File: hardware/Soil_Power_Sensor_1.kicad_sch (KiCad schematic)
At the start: 24 parts, among them J1 Screw_Terminal_01x05, J4 Rsense, U1 THS4532, U2 MAX9944, U3 INA296A, U4 ADS1219

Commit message: Updated board layout
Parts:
- removed J4: Rsense, Connector_PinHeader_2.54mm:PinHeader_1x02_P2.54mm_Vertical, symbol Connector:Conn_01x02_Socket
- RSENSE1: value NC -> DNP
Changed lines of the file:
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@@
   (junction (at 121.92 113.03) (diameter 0) (color 0 0 0 0)
   )
-  (junction (at 35.56 142.24) (diameter 0) (color 0 0 0 0)
-  )
   (junction (at 185.42 99.06) (diameter 0) (color 0 0 0 0)
   )
@@
   (junction (at 87.63 22.86) (diameter 0) (color 0 0 0 0)
   )
-  (junction (at 35.56 132.08) (diameter 0) (color 0 0 0 0)
-  )
   (junction (at 185.42 91.44) (diameter 0) (color 0 0 0 0)
   )
@@
     (stroke (width 0.1524) (type solid))
   )
-  (wire (pts (xy 20.32 132.08) (xy 35.56 132.08))
-    (stroke (width 0) (type default))
-  )
   (wire (pts (xy 124.46 130.81) (xy 121.92 130.81))
     (stroke (width 0.1524) (type solid))
@@
     (stroke (width 0) (type default))
   )
-  (wire (pts (xy 35.56 132.08) (xy 35.56 133.35))
-    (stroke (width 0.1524) (type solid))
-  )
   (wire (pts (xy 254 71.12) (xy 254 73.66))
     (stroke (width 0.1524) (type solid))
@@
     (stroke (width 0.1524) (type solid))
   )
-  (wire (pts (xy 35.56 124.46) (xy 35.56 132.08))
+  (wire (pts (xy 35.56 124.46) (xy 35.56 133.35))
     (stroke (width 0.1524) (type solid))
   )
@@
     (stroke (width 0.1524) (type solid))
   )
-  (wire (pts (xy 20.32 135.89) (xy 20.32 132.08))
-    (stroke (width 0) (type default))
-  )
   (wire (pts (xy 92.71 116.84) (xy 92.71 119.38))
     (stroke (width 0) (type default))
@@
     (stroke (width 0.1524) (type solid))
   )
-  (wire (pts (xy 35.56 140.97) (xy 35.56 142.24))
-    (stroke (width 0.1524) (type solid))
-  )
   (wire (pts (xy 48.26 99.06) (xy 48.26 149.86))
     (stroke (width 0.1524) (type solid))
@@
     (stroke (width 0.1524) (type solid))
   )
-  (wire (pts (xy 20.32 142.24) (xy 35.56 142.24))
-    (stroke (width 0) (type default))
-  )
   (wire (pts (xy 144.78 52.07) (xy 162.56 52.07))
     (stroke (width 0.1524) (type solid))
   )
-  (wire (pts (xy 35.56 142.24) (xy 35.56 149.86))
+  (wire (pts (xy 35.56 140.97) (xy 35.56 149.86))
     (stroke (width 0.1524) (type solid))
   )
   (wire (pts (xy 231.14 71.12) (xy 236.22 71.12))
     (stroke (width 0.1524) (type solid))
-  )
-  (wire (pts (xy 20.32 138.43) (xy 20.32 142.24))
-    (stroke (width 0) (type default))
   )
   (wire (pts (xy 88.9 116.84) (xy 92.71 116.84))
@@
     )
   )
-  (symbol (lib_id "Connector:Conn_01x02_Socket") (at 15.24 138.43 180) (unit 1)
-    (in_bom yes) (on_board yes) (dnp no)
-    (property "Reference" "J4" (at 15.875 130.175 0)
-      (effects (font (size 1.27 1.27)))
-    )
-    (property "Value" "Rsense" (at 15.875 132.715 0)
-      (effects (font (size 1.27 1.27)))
-    )
-    (property "Footprint" "Connector_PinHeader_2.54mm:PinHeader_1x02_P2.54mm_Vertical" (at 15.24 138.43 0)
-      (effects (font (size 1.27 1.27)) hide)
-    )
-    (property "Datasheet" "~" (at 15.24 138.43 0)
-      (effects (font (size 1.27 1.27)) hide)
-    )
-    (pin "1")
-    (pin "2")
-    (instances
-      (project "Soil Power Sensor"
-        (path "/5300ec4d-4648-40a1-8d89-4fa6b3bf32a3/643deee0-b2c1-47dd-8bbd-6697ae8f1315"
-          (reference "J4") (unit 1)
-        )
-      )
-    )
-  )
   (symbol (lib_id "power:GND") (at 254 81.28 0) (unit 1)
     (in_bom yes) (on_board yes) (dnp no)
@@
       (effects (font (size 1.778 1.5113)) (justify left bottom))
     )
-    (property "Value" "NC" (at 33.02 137.16 0)
-      (effects (font (size 1.778 1.5113)) (justify left bottom))
-    )
+    (property "Value" "DNP" (at 33.02 137.16 0)
+      (effects (font (size 1.778 1.5113)) (justify left bottom))
+    )

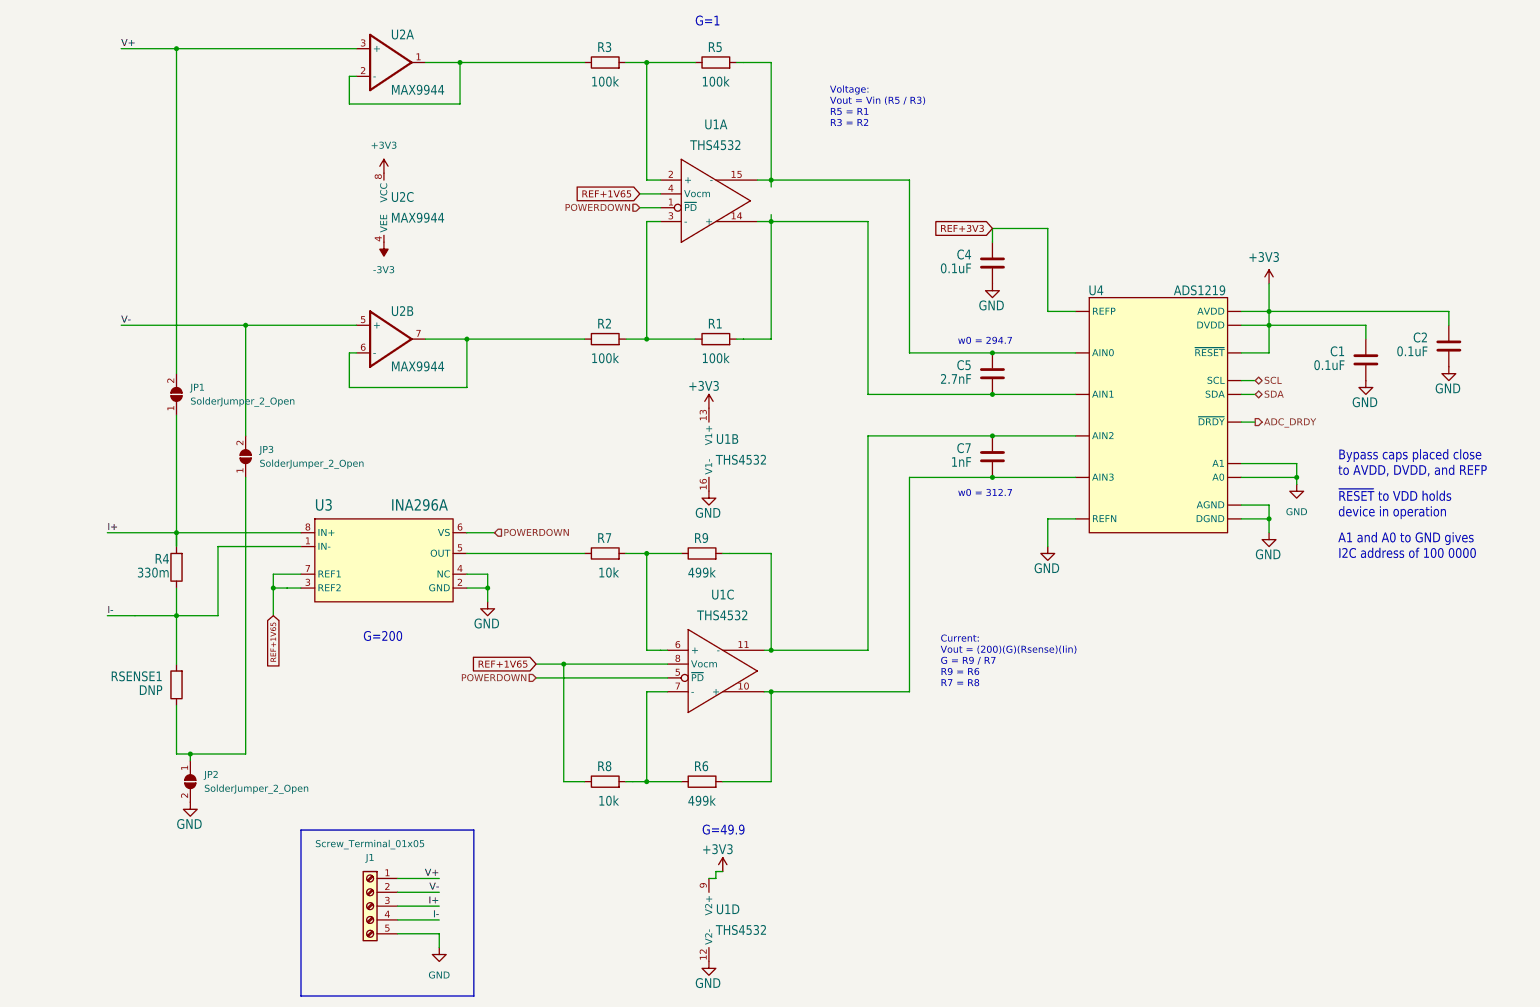
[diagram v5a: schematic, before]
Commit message: Updated annotations based on PCB position
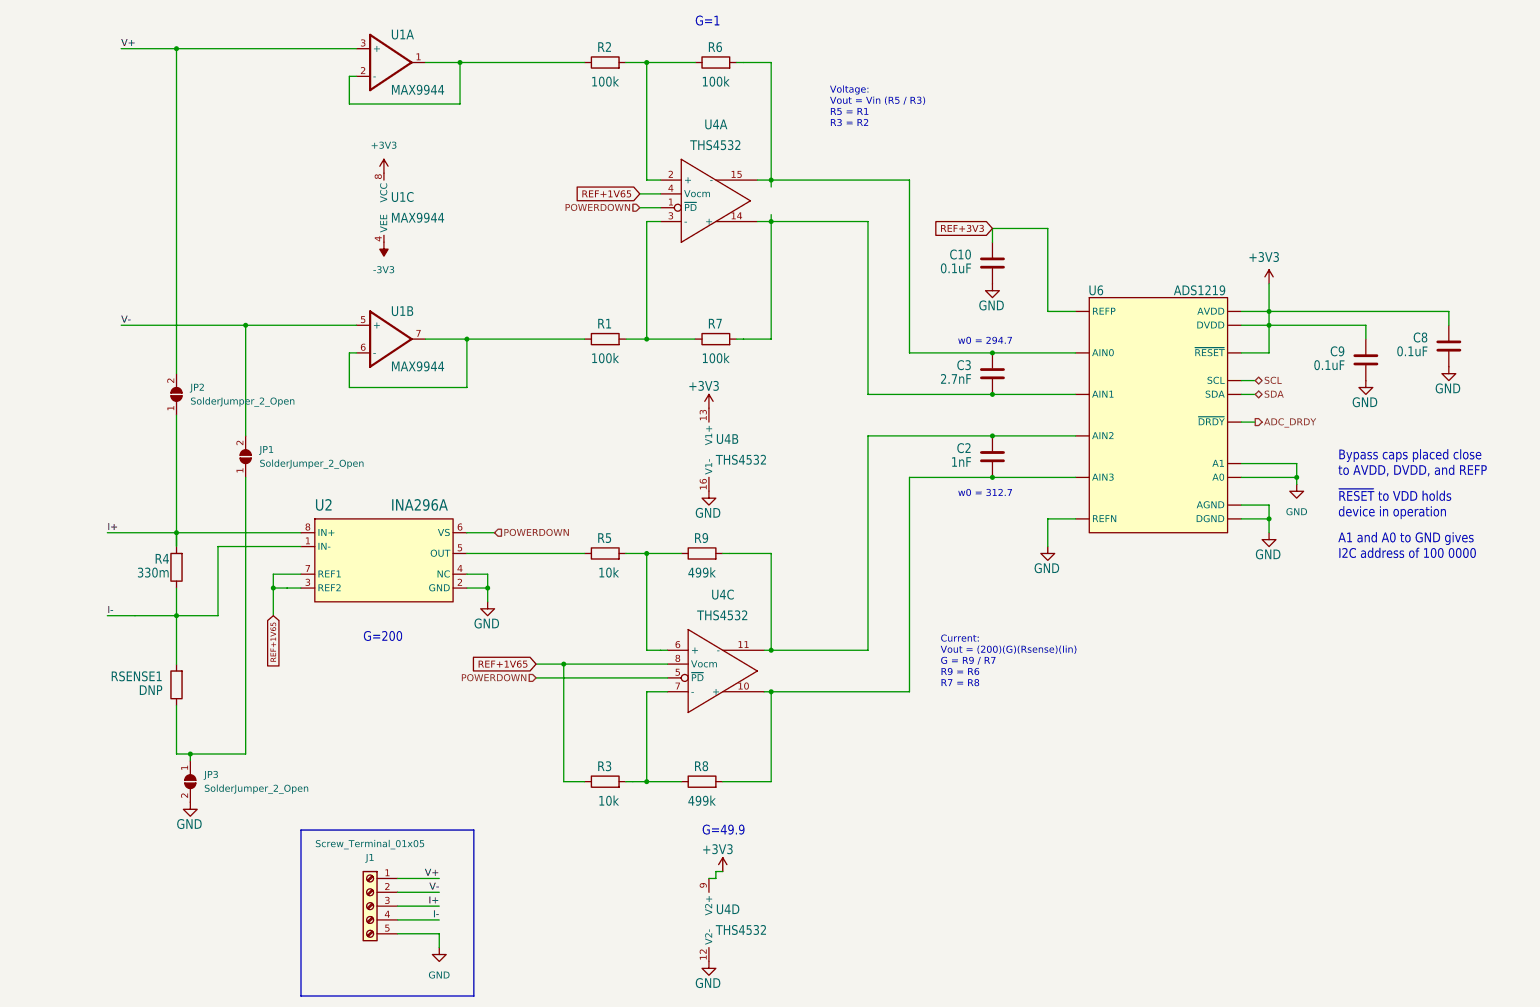
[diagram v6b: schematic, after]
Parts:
- renumbered C4 to C10, C7 to C2, C5 to C3, C2 to C8, C1 to C9, JP3 to JP1, JP1 to JP2, JP2 to JP3, R2 to R1, R3 to R2, R8 to R3, R7 to R5, R5 to R6, R1 to R7, R6 to R8, U2 to U1, U3 to U2, U1 to U4, U4 to U6
